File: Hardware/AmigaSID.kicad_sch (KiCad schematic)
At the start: 40 parts, among them CON1 ZorroII, J1 AudioJack3, J2 SID_AUDIO_OUT, J3 SID_AUDIO_IN, Q1 BC547, U1 74HC688, U2 74LS00, U3 SID, U4 LM7809_TO220, U5 74HC245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

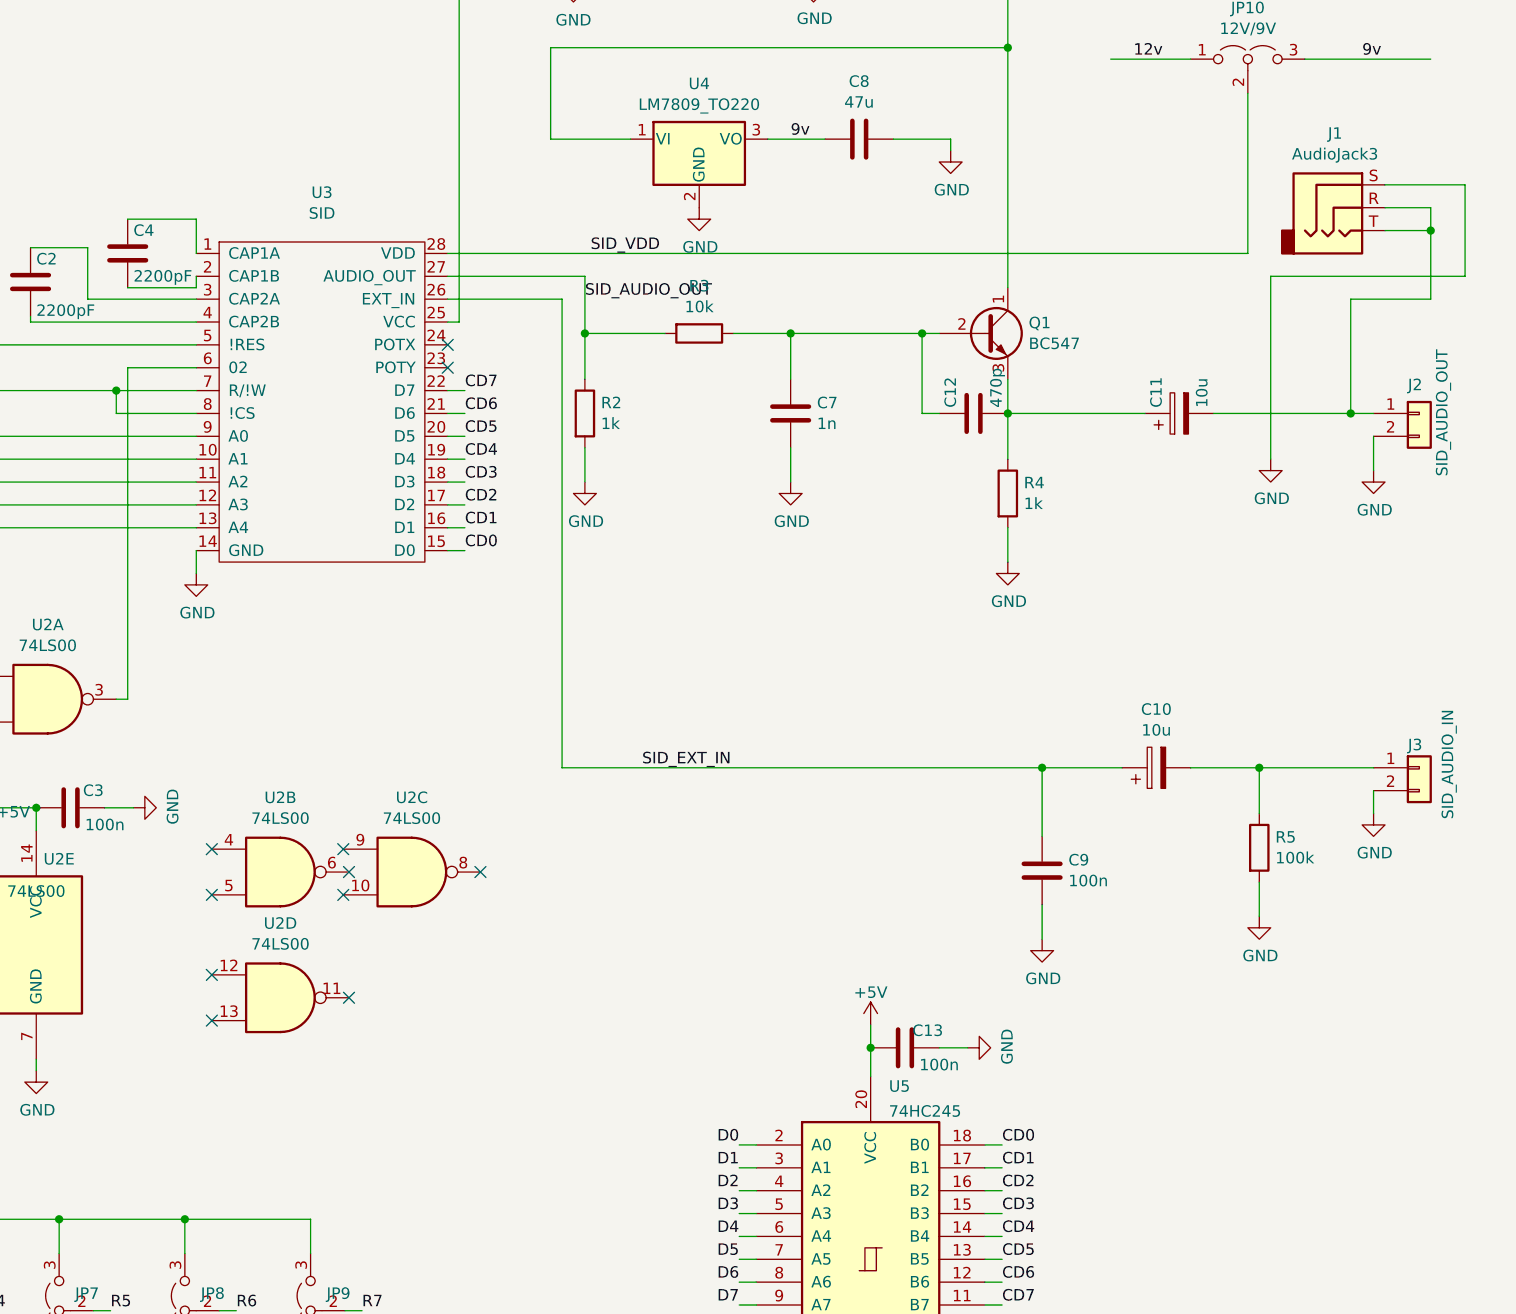
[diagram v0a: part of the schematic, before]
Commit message: - Moved filter caps closer to IC's - Added logo - Floating 245 inputs tied to VCC - Flipped polarity on C10 (SID_AUDIO_IN) - Added jumper to disconnect audio out cap from output pins   - instead you now can fit a little amp board like shown Gadgets video about the original version of the card   - also added one GND and one 12V pin
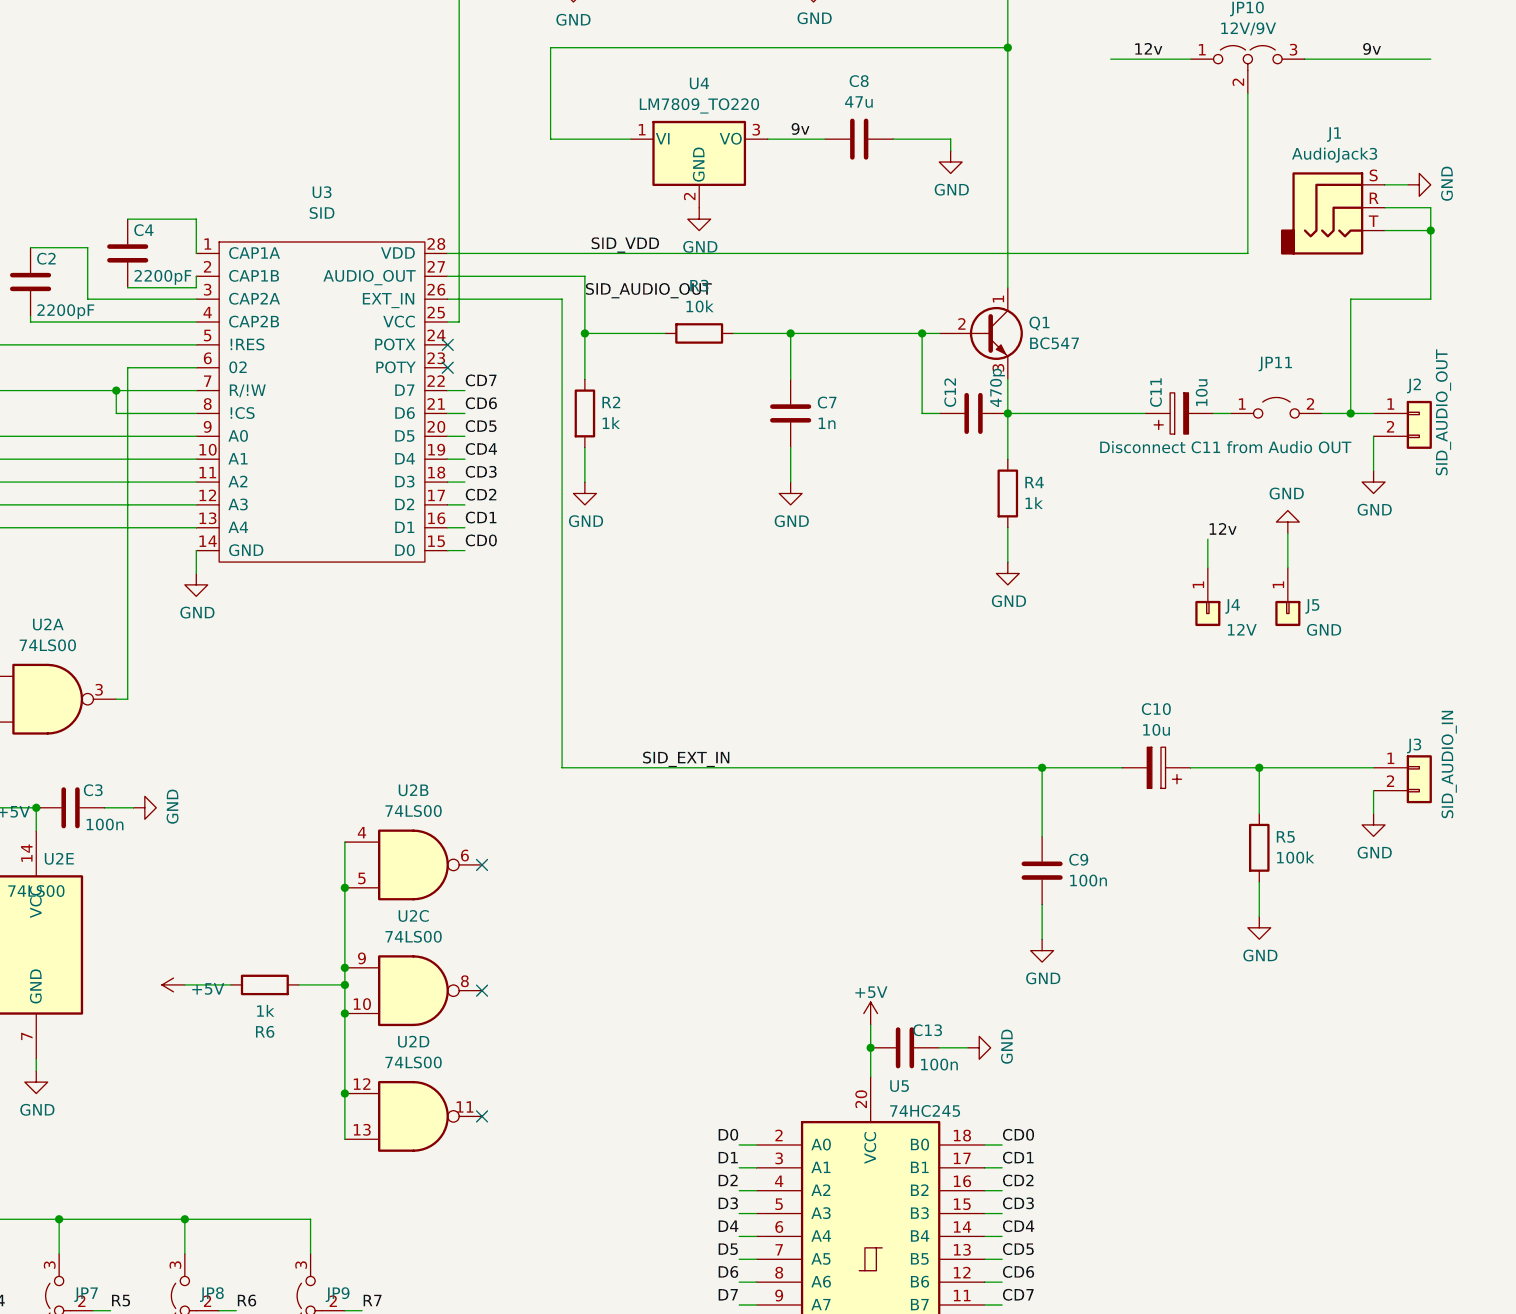
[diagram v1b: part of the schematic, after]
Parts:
- added J4: 12V, Connector_PinHeader_2.54mm:PinHeader_1x01_P2.54mm_Vertical, symbol Connector_Generic:Conn_01x01
- added J5: GND, Connector_PinHeader_2.54mm:PinHeader_1x01_P2.54mm_Vertical, symbol Connector_Generic:Conn_01x01
- added JP11: Disconnect C11 from Audio OUT, Connector_PinHeader_2.54mm:PinHeader_1x02_P2.54mm_Vertical, symbol Jumper:Jumper_2_Open
- added R6: 1k, Resistor_SMD:R_0805_2012Metric_Pad1.20x1.40mm_HandSolder, symbol Device:R
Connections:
- net +5V: now also R6.1
- net 12v: now also J4.1 (Pin_1)
- net GND: now also J5.1 (Pin_1)
- net SID_EXT_IN: now also C10.2; no longer C10.1
- net at J1.R, J1.T, J2.1 (Pin_1): now also JP11.2 (B); no longer C11.2
- net at J3.1 (Pin_1), R5.1: now also C10.1; no longer C10.2
- net at U2.10: now also U2.12, U2.13, U2.4, U2.5, U2.9, R6.2
- new net: C11.2, JP11.1 (A)
- no-connect marks 68 -> 62
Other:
- moved on the sheet: C10, U2B, U2C, U2D

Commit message: Rev2, moved LDO, reset pin for A4k LED and voltage selection jumper, used only basic parts in JLCPCB bom
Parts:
- H1: footprint Connector_Pin:Pin_D0.7mm_L6.5mm_W1.8mm_FlatFork -> Connector_PinHeader_2.54mm:PinHeader_1x01_P2.54mm_Vertical
- JP10: footprint Connector_PinHeader_2.54mm:PinHeader_1x03_P2.54mm_Vertical -> Connector_PinHeader_2.54mm:PinHeader_1x03_P2.54mm_Horizontal
- U4: footprint Package_TO_SOT_THT:TO-220-3_Vertical -> Package_TO_SOT_THT:TO-220-3_Horizontal_TabDown
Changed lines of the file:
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@@
 (kicad_sch (version 20211123) (generator eeschema)
   (paper "A3")
+  (title_block
+    (rev "2")
+  )
   (junction (at 326.39 110.49) (diameter 0) (color 0 0 0 0)
   )
@@
     (property "Reference" "H1" (id 0) (at 100.2538 105.7402 90))
     (property "Value" "SID_/RST" (id 1) (at 100.2538 108.0516 90))
-    (property "Footprint" "Connector_Pin:Pin_D0.7mm_L6.5mm_W1.8mm_FlatFork" (id 2) (at 100.33 111.76 0)
+    (property "Footprint" "Connector_PinHeader_2.54mm:PinHeader_1x01_P2.54mm_Vertical" (id 2) (at 100.33 111.76 0)
       (effects (font (size 1.27 1.27)) hide)
     )
@@
     (property "Reference" "U4" (id 0) (at 316.23 82.7532 0))
     (property "Value" "LM7809_TO220" (id 1) (at 316.23 85.0646 0))
-    (property "Footprint" "Package_TO_SOT_THT:TO-220-3_Vertical" (id 2) (at 316.23 83.185 0)
+    (property "Footprint" "Package_TO_SOT_THT:TO-220-3_Horizontal_TabDown" (id 2) (at 316.23 83.185 0)
       (effects (font (size 1.27 1.27) italic) hide)
     )
@@
     (property "Reference" "JP10" (id 0) (at 377.19 74.3204 0))
     (property "Value" "12V/9V" (id 1) (at 377.19 76.6318 0))
-    (property "Footprint" "Connector_PinHeader_2.54mm:PinHeader_1x03_P2.54mm_Vertical" (id 2) (at 377.19 80.01 0)
+    (property "Footprint" "Connector_PinHeader_2.54mm:PinHeader_1x03_P2.54mm_Horizontal" (id 2) (at 377.19 80.01 0)
       (effects (font (size 1.27 1.27)) hide)
     )
@@
     )
     (path "/00000000-0000-0000-0000-00005fb3d287"
-      (reference "H1") (unit 1) (value "SID_/RST") (footprint "Connector_Pin:Pin_D0.7mm_L6.5mm_W1.8mm_FlatFork")
+      (reference "H1") (unit 1) (value "SID_/RST") (footprint "Connector_PinHeader_2.54mm:PinHeader_1x01_P2.54mm_Vertical")
     )
     (path "/00000000-0000-0000-0000-00005fd024e7"
@@
     )
     (path "/00000000-0000-0000-0000-00005fc18e65"
-      (reference "JP10") (unit 1) (value "12V/9V") (footprint "Connector_PinHeader_2.54mm:PinHeader_1x03_P2.54mm_Vertical")
+      (reference "JP10") (unit 1) (value "12V/9V") (footprint "Connector_PinHeader_2.54mm:PinHeader_1x03_P2.54mm_Horizontal")
     )
     (path "/126aec73-f420-4da1-a51b-89f22b12639d"
@@
     )
     (path "/00000000-0000-0000-0000-00005fbb894c"
-      (reference "U4") (unit 1) (value "LM7809_TO220") (footprint "Package_TO_SOT_THT:TO-220-3_Vertical")
+      (reference "U4") (unit 1) (value "LM7809_TO220") (footprint "Package_TO_SOT_THT:TO-220-3_Horizontal_TabDown")
     )
     (path "/747da935-1933-4026-b877-fa1c87754b64"
